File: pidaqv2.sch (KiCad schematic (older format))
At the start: 10 parts, among them J101 Screw_Terminal_01x11, J102 Screw_Terminal_01x06, J103 Conn_01x02_Male, J104 Screw_Terminal_01x08, J105 Screw_Terminal_01x04

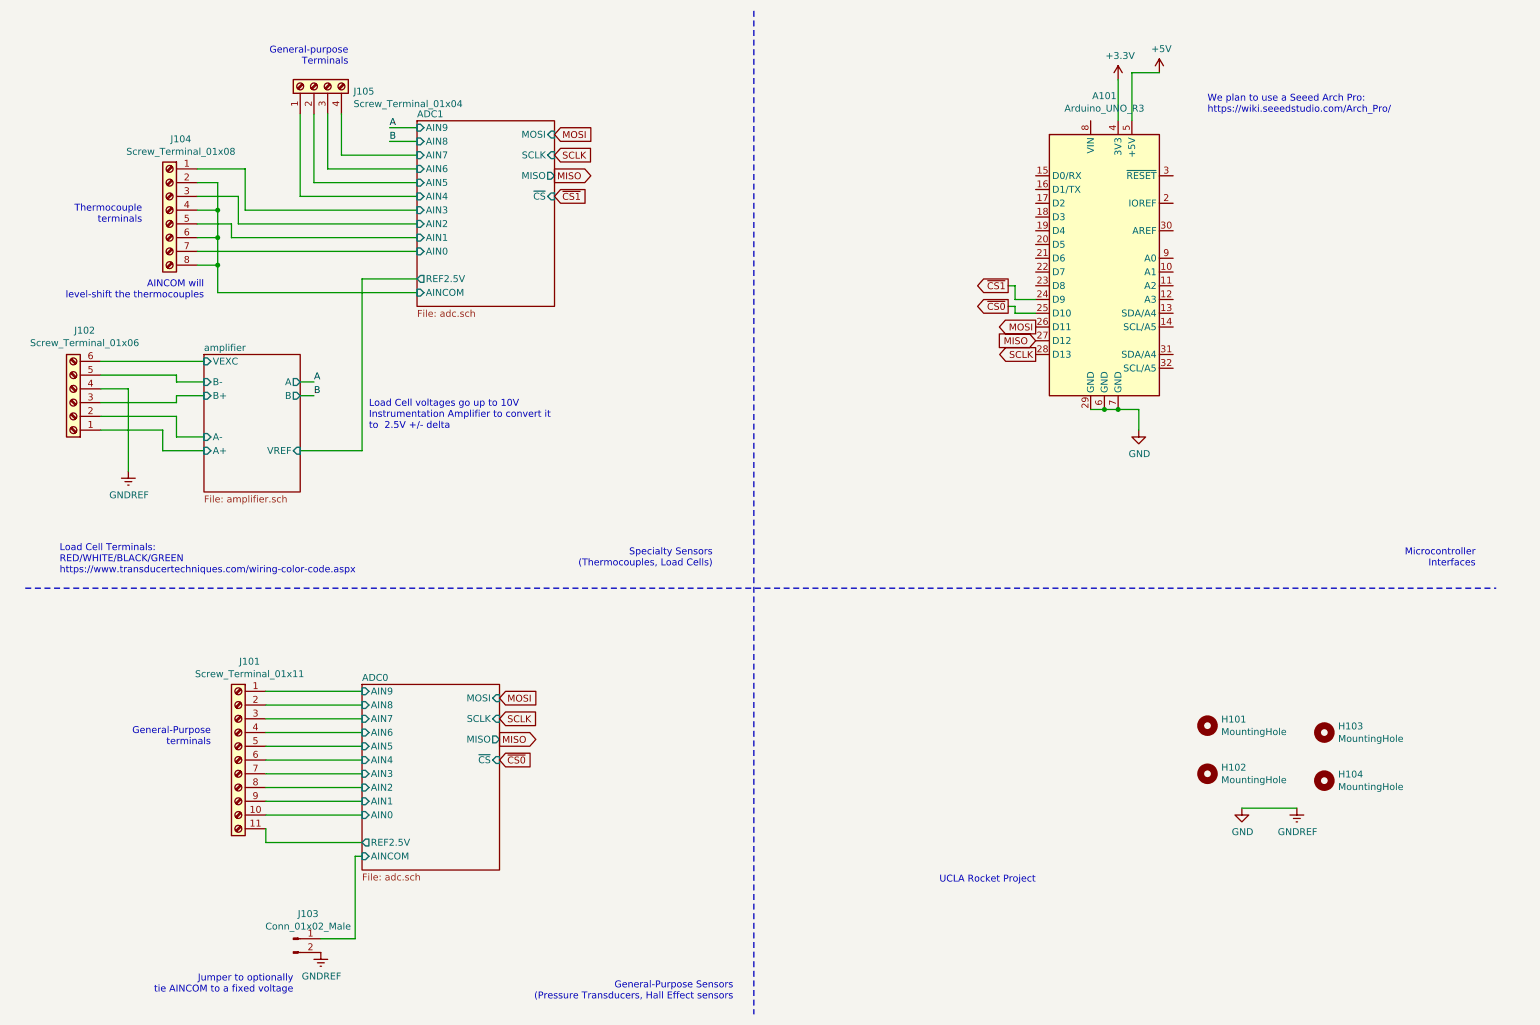
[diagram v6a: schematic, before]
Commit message: add silkscreen labels
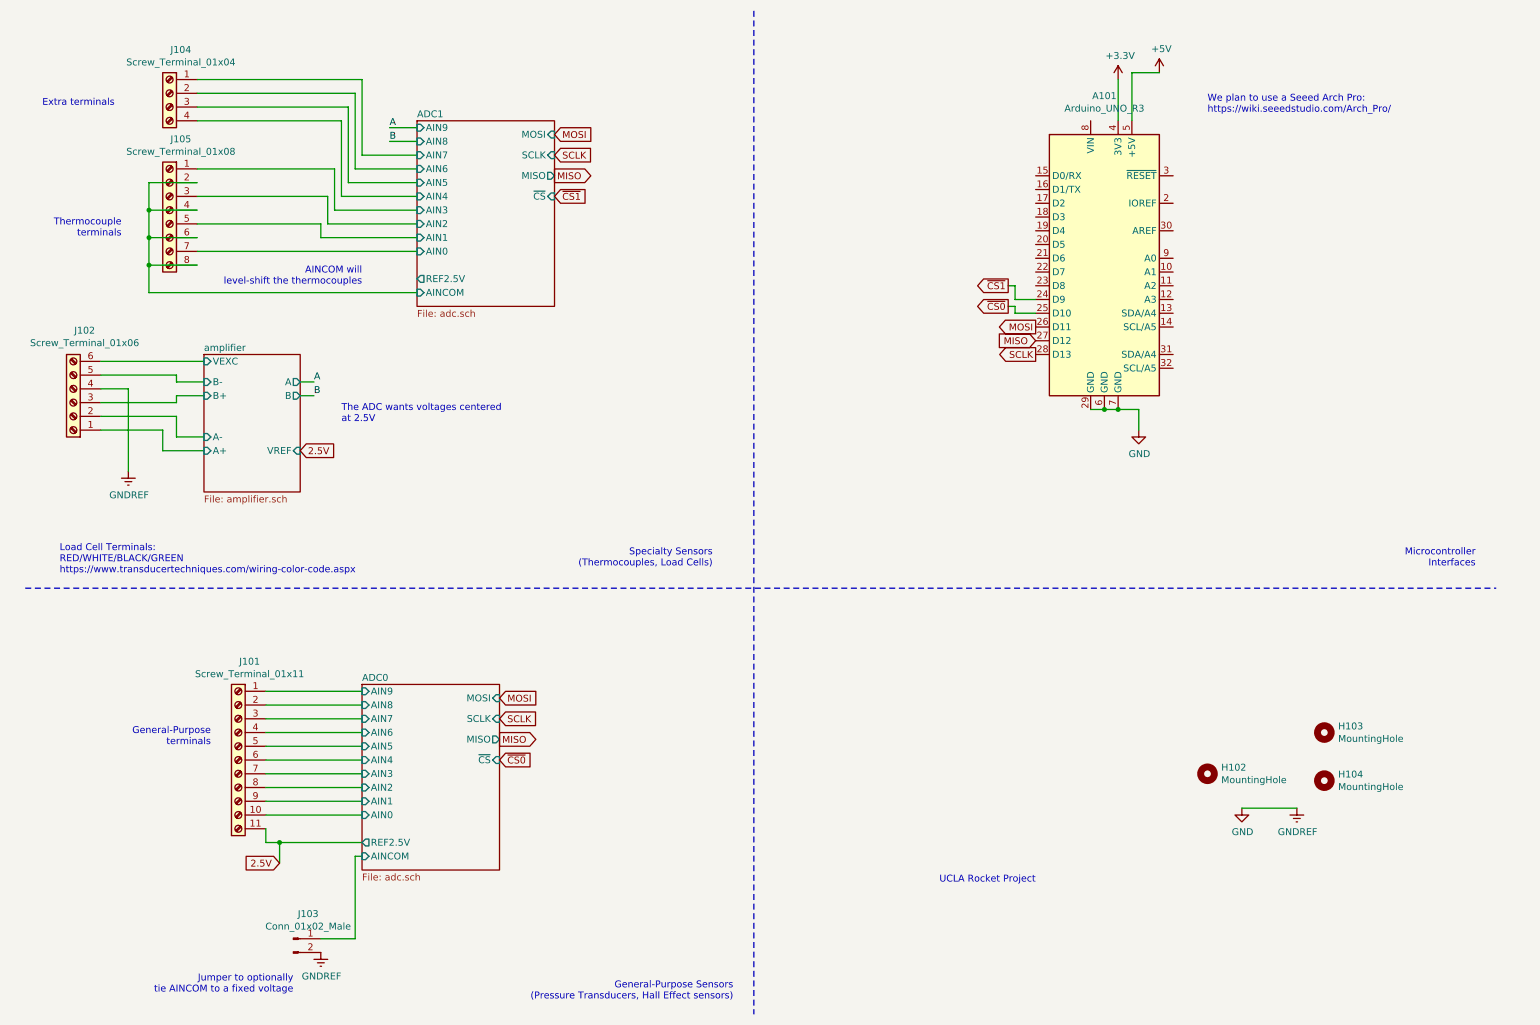
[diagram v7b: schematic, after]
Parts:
- removed H101: MountingHole, MountingHole:MountingHole_3.2mm_M3_ISO7380, symbol Mechanical:MountingHole
- removed J104: Screw_Terminal_01x08, TerminalBlock_Phoenix:TerminalBlock_Phoenix_MPT-0,5-8-2.54_1x08_P2.54mm_Horizontal, symbol Connector:Screw_Terminal_01x08
- removed J105: Screw_Terminal_01x04, TerminalBlock_Phoenix:TerminalBlock_Phoenix_MPT-0,5-4-2.54_1x04_P2.54mm_Horizontal, symbol Connector:Screw_Terminal_01x04
- added J104: Screw_Terminal_01x04, TerminalBlock_TE-Connectivity:TerminalBlock_TE_282834-4_1x04_P2.54mm_Horizontal, symbol Connector:Screw_Terminal_01x04
- added J105: Screw_Terminal_01x08, TerminalBlock_TE-Connectivity:TerminalBlock_TE_282834-8_1x08_P2.54mm_Horizontal, symbol Connector:Screw_Terminal_01x08
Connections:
- net ADC1/AIN0: now also J105.7 (Pin_7)
- net ADC1/AIN1: now also J105.5 (Pin_5)
- net ADC1/AIN2: now also J105.3 (Pin_3)
- net ADC1/AIN3: now also J105.1 (Pin_1)
- net ADC1/AIN4: now also J104.4 (Pin_4)
- net ADC1/AIN5: now also J104.3 (Pin_3)
- net ADC1/AIN6: now also J104.2 (Pin_2)
- net ADC1/AIN7: now also J104.1 (Pin_1)
- net ADC1/AINCOM: now also J105.2 (Pin_2), J105.4 (Pin_4), J105.6 (Pin_6), J105.8 (Pin_8)
- net ADC0/REF2.5V renamed 2.5V
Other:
- note added: "Extra terminals"
- note added: "General-Purpose Sensors\n(Pressure Transducers, Hall Effect sensors)"
- note added: "The ADC wants voltages centered\nat 2.5V"
- note removed: "General-Purpose Sensors\n(Pressure Transducers, Hall Effect sensors"
- note removed: "General-purpose\nTerminals"
- note removed: "Load Cell voltages go up to 10V\nInstrumentation Amplifier to convert it\nto 2.5V +/- delta"
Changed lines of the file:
@@
-$EndComp
-$Comp
-L Mechanical:MountingHole H101
-U 1 1 5F4F27FC
-P 9100 5700
-F 0 "H101" H 9200 5746 50  0000 L CNN
-F 1 "MountingHole" H 9200 5655 50  0000 L CNN
-F 2 "MountingHole:MountingHole_3.2mm_M3_ISO7380" H 9100 5700 50  0001 C CNN
-F 3 "~" H 9100 5700 50  0001 C CNN
-	1    9100 5700
-	1    0    0    -1
 $EndComp
 $Comp
@@
 F9 "VREF" I R 2500 3700 50
 $EndSheet
-Text Notes 3000 3550 0    50   ~ 0
-Load Cell voltages go up to 10V\nInstrumentation Amplifier to convert it\nto  2.5V +/- delta
+Text Notes 2800 3500 0    50   ~ 0
+The ADC wants voltages centered\nat 2.5V
 $Comp
 L Connector:Screw_Terminal_01x11 J101
@@
 Jumper to optionally\ntie AINCOM to a fixed voltage
 $Comp
-L Connector:Screw_Terminal_01x08 J104
-U 1 1 5F6B71F7
-P 1550 1950
-F 0 "J104" H 1468 2467 50  0000 C CNN
-F 1 "Screw_Terminal_01x08" H 1468 2376 50  0000 C CNN
-F 2 "TerminalBlock_Phoenix:TerminalBlock_Phoenix_MPT-0,5-8-2.54_1x08_P2.54mm_Horizontal" H 1550 1950 50  0001 C CNN
-F 3 "~" H 1550 1950 50  0001 C CNN
-	1    1550 1950
-	-1   0    0    -1
-$EndComp
-$Comp
 L power:GNDREF #PWR0114
 U 1 1 5F6C0CC4
@@
 Wire Wire Line
 	2500 3200 2600 3200
-Text Notes 1800 2600 2    50   ~ 0
+Text Notes 2950 2500 2    50   ~ 0
 AINCOM will \nlevel-shift the thermocouples\n
-Wire Wire Line
-	3350 2450 2950 2450
-Wire Wire Line
-	2950 2450 2950 3700
-Wire Wire Line
-	2950 3700 2500 3700
-Wire Wire Line
-	3350 2050 2050 2050
-Wire Wire Line
-	3350 1950 2100 1950
-$Comp
-L Connector:Screw_Terminal_01x04 J105
-U 1 1 5F75BDB3
-P 2600 1050
-F 0 "J105" V 2564 762 50  0000 R CNN
-F 1 "Screw_Terminal_01x04" V 2473 762 50  0000 R CNN
-F 2 "TerminalBlock_Phoenix:TerminalBlock_Phoenix_MPT-0,5-4-2.54_1x04_P2.54mm_Horizontal" H 2600 1050 50  0001 C CNN
-F 3 "~" H 2600 1050 50  0001 C CNN
-	1    2600 1050
-	0    -1   -1   0
-$EndComp
-Wire Wire Line
-	3350 1550 2800 1550
-Wire Wire Line
-	2800 1550 2800 1250
-Wire Wire Line
-	2700 1250 2700 1650
-Wire Wire Line
-	2700 1650 3350 1650
-Wire Wire Line
-	3350 1750 2600 1750
-Wire Wire Line
-	2600 1750 2600 1250
-Wire Wire Line
-	2500 1250 2500 1850
-Wire Wire Line
-	2500 1850 3350 1850
-Text Notes 1350 2050 2    50   ~ 0
+Text Notes 1200 2150 2    50   ~ 0
 Thermocouple\nterminals
-Text Notes 2850 900  2    50   ~ 0
-General-purpose\nTerminals
 Text Notes 1850 5850 2    50   ~ 0
 General-Purpose\nterminals
@@
 	5800 500  5800 7800
 Text Notes 5650 7700 2    50   ~ 0
-General-Purpose Sensors\n(Pressure Transducers, Hall Effect sensors
+General-Purpose Sensors\n(Pressure Transducers, Hall Effect sensors)
 Wire Notes Line
 	500  4700 11200 4700
 Text Notes 11050 4550 2    50   ~ 0
 Microcontroller\nInterfaces
-Wire Wire Line
-	1750 2350 1900 2350
-Wire Wire Line
-	1750 2150 1900 2150
-Wire Wire Line
-	1900 2150 1900 2350
-Wire Wire Line
-	1750 1950 1900 1950
-Wire Wire Line
-	1900 1950 1900 2150
-Connection ~ 1900 2150
-Wire Wire Line
-	1750 1750 1900 1750
-Wire Wire Line
-	1900 1750 1900 1950
-Connection ~ 1900 1950
-Wire Wire Line
-	1750 1650 2100 1650
-Wire Wire Line
-	2100 1650 2100 1950
-Wire Wire Line
-	1750 1850 2050 1850
-Wire Wire Line
-	2050 1850 2050 2050
-Wire Wire Line
-	1750 2050 2000 2050
-Wire Wire Line
-	2000 2050 2000 2150
-Wire Wire Line
-	2000 2150 3350 2150
-Wire Wire Line
-	1750 2250 3350 2250
 Text Label 2600 3200 0    50   ~ 0
 A
@@
 B
 Wire Wire Line
-	2250 6550 2950 6550
+	2250 6550 2350 6550
 $Comp
 L Connector:Conn_01x02_Male J103
@@
 We plan to use a Seeed Arch Pro:\nhttps://wiki.seeedstudio.com/Arch_Pro/
 Wire Wire Line
-	3350 2550 1900 2550
-Wire Wire Line
-	1900 2550 1900 2350
-Connection ~ 1900 2350
-Wire Wire Line
 	2500 3300 2600 3300
 Text Label 3150 1350 0    50   ~ 0
@@
 Wire Wire Line
 	3150 1450 3350 1450
+Text GLabel 2350 6700 0    50   Input ~ 0
+2.5V
+Wire Wire Line
+	2350 6550 2350 6700
+Connection ~ 2350 6550
+Wire Wire Line
+	2350 6550 2950 6550
+Text GLabel 2500 3700 2    50   Input ~ 0
+2.5V
+Wire Wire Line
+	3350 1550 2950 1550
+Wire Wire Line
+	2950 1550 2950 1000
+Wire Wire Line
+	3350 1650 2900 1650
+Wire Wire Line
+	2900 1650 2900 1100
+Wire Wire Line
+	3350 1750 2850 1750
+Wire Wire Line
+	3350 1850 2800 1850
+Wire Wire Line
+	3350 1950 2750 1950
+Wire Wire Line
+	2750 1950 2750 1650
+Wire Wire Line
+	2750 1650 1750 1650
+Wire Wire Line
+	3350 2050 2700 2050
+Wire Wire Line
+	2700 2050 2700 1850
+Wire Wire Line
+	2700 1850 1750 1850
+Wire Wire Line
+	3350 2150 2650 2150
+Wire Wire Line
+	2650 2150 2650 2050
+Wire Wire Line
+	2650 2050 1750 2050
+Wire Wire Line
+	3350 2250 1750 2250
+Wire Wire Line
+	1400 2550 1400 2350
+Wire Wire Line
+	1400 2350 1750 2350
+Wire Wire Line
+	1400 2550 3350 2550
+Wire Wire Line
+	1400 2350 1400 2150
+Connection ~ 1400 2350
+Wire Wire Line
+	1750 2150 1400 2150
+Connection ~ 1400 2150
+Wire Wire Line
+	1400 2150 1400 1950
+Wire Wire Line
+	1750 1950 1400 1950
+Connection ~ 1400 1950
+Wire Wire Line
+	1400 1950 1400 1750
+Wire Wire Line
+	1750 1750 1400 1750
+$Comp
+L Connector:Screw_Terminal_01x08 J105
+U 1 1 5F6FB13F
+P 1550 1950
+F 0 "J105" H 1468 2467 50  0000 C CNN
+F 1 "Screw_Terminal_01x08" H 1468 2376 50  0000 C CNN
+F 2 "TerminalBlock_TE-Connectivity:TerminalBlock_TE_282834-8_1x08_P2.54mm_Horizontal" H 1550 1950 50  0001 C CNN
+F 3 "~" H 1550 1950 50  0001 C CNN
+	1    1550 1950
+	-1   0    0    -1
+$EndComp
+$Comp
+L Connector:Screw_Terminal_01x04 J104
+U 1 1 5F7080E0
+P 1550 1100
+F 0 "J104" H 1468 1417 50  0000 C CNN
+F 1 "Screw_Terminal_01x04" H 1468 1326 50  0000 C CNN
+F 2 "TerminalBlock_TE-Connectivity:TerminalBlock_TE_282834-4_1x04_P2.54mm_Horizontal" H 1550 1100 50  0001 C CNN
+F 3 "~" H 1550 1100 50  0001 C CNN
+	1    1550 1100
+	-1   0    0    -1
+$EndComp
+Wire Wire Line
+	2800 1300 1750 1300
+Wire Wire Line
+	2800 1300 2800 1850
+Wire Wire Line
+	1750 1200 2850 1200
+Wire Wire Line
+	2850 1200 2850 1750
+Wire Wire Line
+	1750 1100 2900 1100
+Wire Wire Line
+	1750 1000 2950 1000
+Text Notes 1150 1200 2    50   ~ 0
+Extra terminals
 $EndSCHEMATC

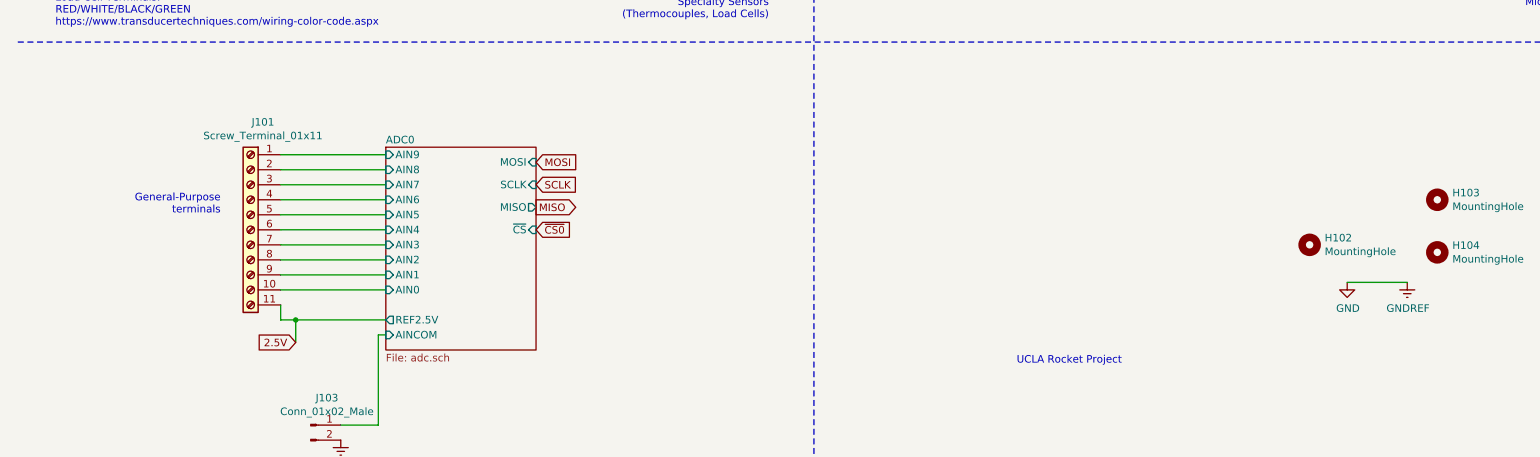
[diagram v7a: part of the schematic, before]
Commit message: placed general sensors chip
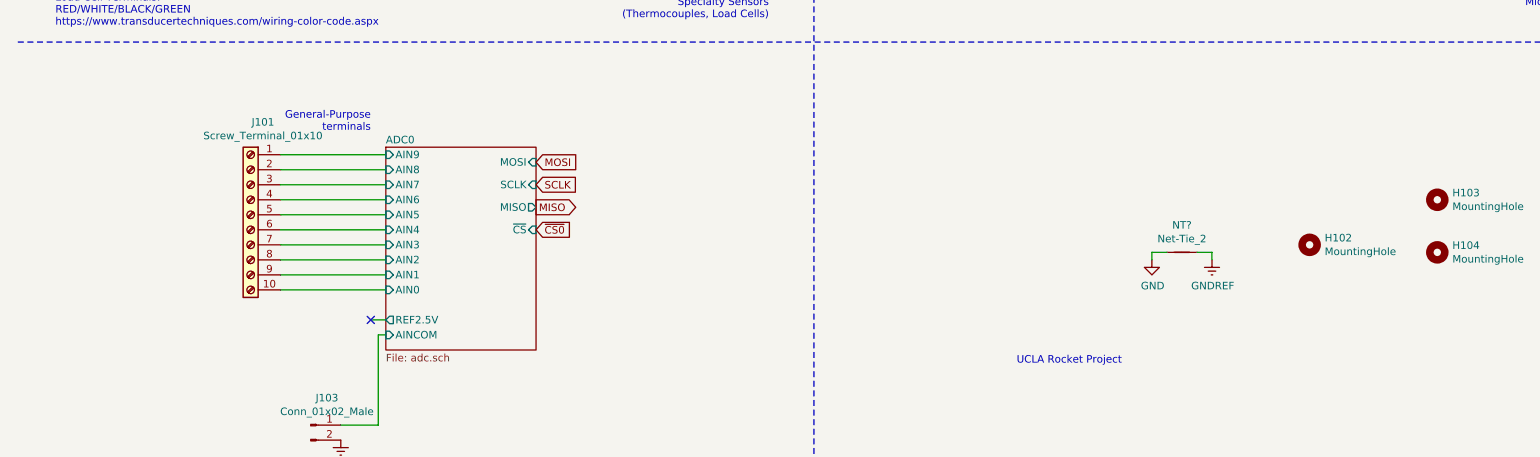
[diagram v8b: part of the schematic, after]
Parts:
- removed J101: Screw_Terminal_01x11, TerminalBlock_Phoenix:TerminalBlock_Phoenix_MKDS-3-11-5.08_1x11_P5.08mm_Horizontal, symbol Connector:Screw_Terminal_01x11
- added J101: Screw_Terminal_01x10, TerminalBlock_TE-Connectivity:TerminalBlock_TE_1-282834-0_1x10_P2.54mm_Horizontal, symbol Connector:Screw_Terminal_01x10
- added NT?: Net-Tie_2, symbol Device:Net-Tie_2
- J102: footprint TerminalBlock_Phoenix:TerminalBlock_Phoenix_MKDS-1,5-6-5.08_1x06_P5.08mm_Horizontal -> TerminalBlock_TE-Connectivity:TerminalBlock_TE_282834-6_1x06_P2.54mm_Horizontal
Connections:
- net ADC0/AIN0: now also J101.10 (Pin_10)
- net ADC0/AIN1: now also J101.9 (Pin_9)
- net ADC0/AIN2: now also J101.8 (Pin_8)
- net ADC0/AIN3: now also J101.7 (Pin_7)
- net ADC0/AIN4: now also J101.6 (Pin_6)
- net ADC0/AIN5: now also J101.5 (Pin_5)
- net ADC0/AIN6: now also J101.4 (Pin_4)
- net ADC0/AIN7: now also J101.3 (Pin_3)
- net ADC0/AIN8: now also J101.2 (Pin_2)
- net ADC0/AIN9: now also J101.1 (Pin_1)
- net GND: now also NT?.1; no longer J102.4 (Pin_4), J103.2 (Pin_2)
- new net GNDREF: J102.4 (Pin_4), J103.2 (Pin_2), NT?.2
- no-connect marks 0 -> 1
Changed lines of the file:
@@
 L power:GND #PWR0140
 U 1 1 5F5461E4
-P 9350 6300
-F 0 "#PWR0140" H 9350 6050 50  0001 C CNN
-F 1 "GND" H 9355 6127 50  0000 C CNN
-F 2 "" H 9350 6300 50  0001 C CNN
-F 3 "" H 9350 6300 50  0001 C CNN
-	1    9350 6300
+P 8050 6150
+F 0 "#PWR0140" H 8050 5900 50  0001 C CNN
+F 1 "GND" H 8055 5977 50  0000 C CNN
+F 2 "" H 8050 6150 50  0001 C CNN
+F 3 "" H 8050 6150 50  0001 C CNN
+	1    8050 6150
 	1    0    0    -1
 $EndComp
@@
 L power:GNDREF #PWR0141
 U 1 1 5F547373
-P 9750 6300
-F 0 "#PWR0141" H 9750 6050 50  0001 C CNN
-F 1 "GNDREF" H 9755 6127 50  0000 C CNN
-F 2 "" H 9750 6300 50  0001 C CNN
-F 3 "" H 9750 6300 50  0001 C CNN
-	1    9750 6300
-	1    0    0    -1
-$EndComp
-Wire Wire Line
-	9350 6300 9750 6300
+P 8450 6150
+F 0 "#PWR0141" H 8450 5900 50  0001 C CNN
+F 1 "GNDREF" H 8455 5977 50  0000 C CNN
+F 2 "" H 8450 6150 50  0001 C CNN
+F 3 "" H 8450 6150 50  0001 C CNN
+	1    8450 6150
+	1    0    0    -1
+$EndComp
 $Comp
 L Mechanical:MountingHole H103
@@
 Text Notes 2800 3500 0    50   ~ 0
 The ADC wants voltages centered\nat 2.5V
-$Comp
-L Connector:Screw_Terminal_01x11 J101
-U 1 1 5F6ADD6F
-P 2050 5950
-F 0 "J101" H 1968 6667 50  0000 C CNN
-F 1 "Screw_Terminal_01x11" H 1968 6576 50  0000 C CNN
-F 2 "TerminalBlock_Phoenix:TerminalBlock_Phoenix_MKDS-3-11-5.08_1x11_P5.08mm_Horizontal" H 2050 5950 50  0001 C CNN
-F 3 "~" H 2050 5950 50  0001 C CNN
-	1    2050 5950
-	-1   0    0    -1
-$EndComp
 Wire Wire Line
 	2950 6650 2900 6650
@@
 	1600 3600 1800 3600
 Wire Wire Line
-	2250 6550 2250 6450
-Wire Wire Line
 	2250 6350 2950 6350
 Wire Wire Line
@@
 Text Notes 1200 2150 2    50   ~ 0
 Thermocouple\nterminals
-Text Notes 1850 5850 2    50   ~ 0
+Text Notes 2850 5300 2    50   ~ 0
 General-Purpose\nterminals
 Text Notes 7850 6850 2    50   ~ 0
@@
 Text Label 2600 3300 0    50   ~ 0
 B
-Wire Wire Line
-	2250 6550 2350 6550
 $Comp
 L Connector:Conn_01x02_Male J103
@@
 F 0 "J102" H 768 2825 50  0000 C CNN
 F 1 "Screw_Terminal_01x06" H 768 2916 50  0000 C CNN
-F 2 "TerminalBlock_Phoenix:TerminalBlock_Phoenix_MKDS-1,5-6-5.08_1x06_P5.08mm_Horizontal" H 850 3350 50  0001 C CNN
+F 2 "TerminalBlock_TE-Connectivity:TerminalBlock_TE_282834-6_1x06_P2.54mm_Horizontal" H 850 3350 50  0001 C CNN
 F 3 "~" H 850 3350 50  0001 C CNN
 	1    850  3350
@@
 Wire Wire Line
 	3150 1450 3350 1450
-Text GLabel 2350 6700 0    50   Input ~ 0
-2.5V
-Wire Wire Line
-	2350 6550 2350 6700
-Connection ~ 2350 6550
-Wire Wire Line
-	2350 6550 2950 6550
 Text GLabel 2500 3700 2    50   Input ~ 0
 2.5V
@@
 Text Notes 1150 1200 2    50   ~ 0
 Extra terminals
+$Comp
+L Connector:Screw_Terminal_01x10 J101
+U 1 1 5F785590
+P 2050 5850
+F 0 "J101" H 1968 6467 50  0000 C CNN
+F 1 "Screw_Terminal_01x10" H 1968 6376 50  0000 C CNN
+F 2 "TerminalBlock_TE-Connectivity:TerminalBlock_TE_1-282834-0_1x10_P2.54mm_Horizontal" H 2050 5850 50  0001 C CNN
+F 3 "~" H 2050 5850 50  0001 C CNN
+	1    2050 5850
+	-1   0    0    -1
+$EndComp
+Wire Wire Line
+	2950 6550 2850 6550
+NoConn ~ 2850 6550
+$Comp
+L Device:Net-Tie_2 NT?
+U 1 1 5F799F68
+P 8250 6100
+F 0 "NT?" H 8250 6281 50  0000 C CNN
+F 1 "Net-Tie_2" H 8250 6190 50  0000 C CNN
+F 2 "" H 8250 6100 50  0001 C CNN
+F 3 "~" H 8250 6100 50  0001 C CNN
+	1    8250 6100
+	1    0    0    -1
+$EndComp
+Wire Wire Line
+	8050 6150 8050 6100
+Wire Wire Line
+	8050 6100 8150 6100
+Wire Wire Line
+	8350 6100 8450 6100
+Wire Wire Line
+	8450 6100 8450 6150
 $EndSCHEMATC
